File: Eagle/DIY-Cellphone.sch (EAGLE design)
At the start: 66 parts, among them IC1 MEGA1284, J1 ISP, U1 MCP73831, U7 M10_HDWITHOUT_EXCLUSION, X1 BU-SMA-V, X3 CCM03-3002 R102

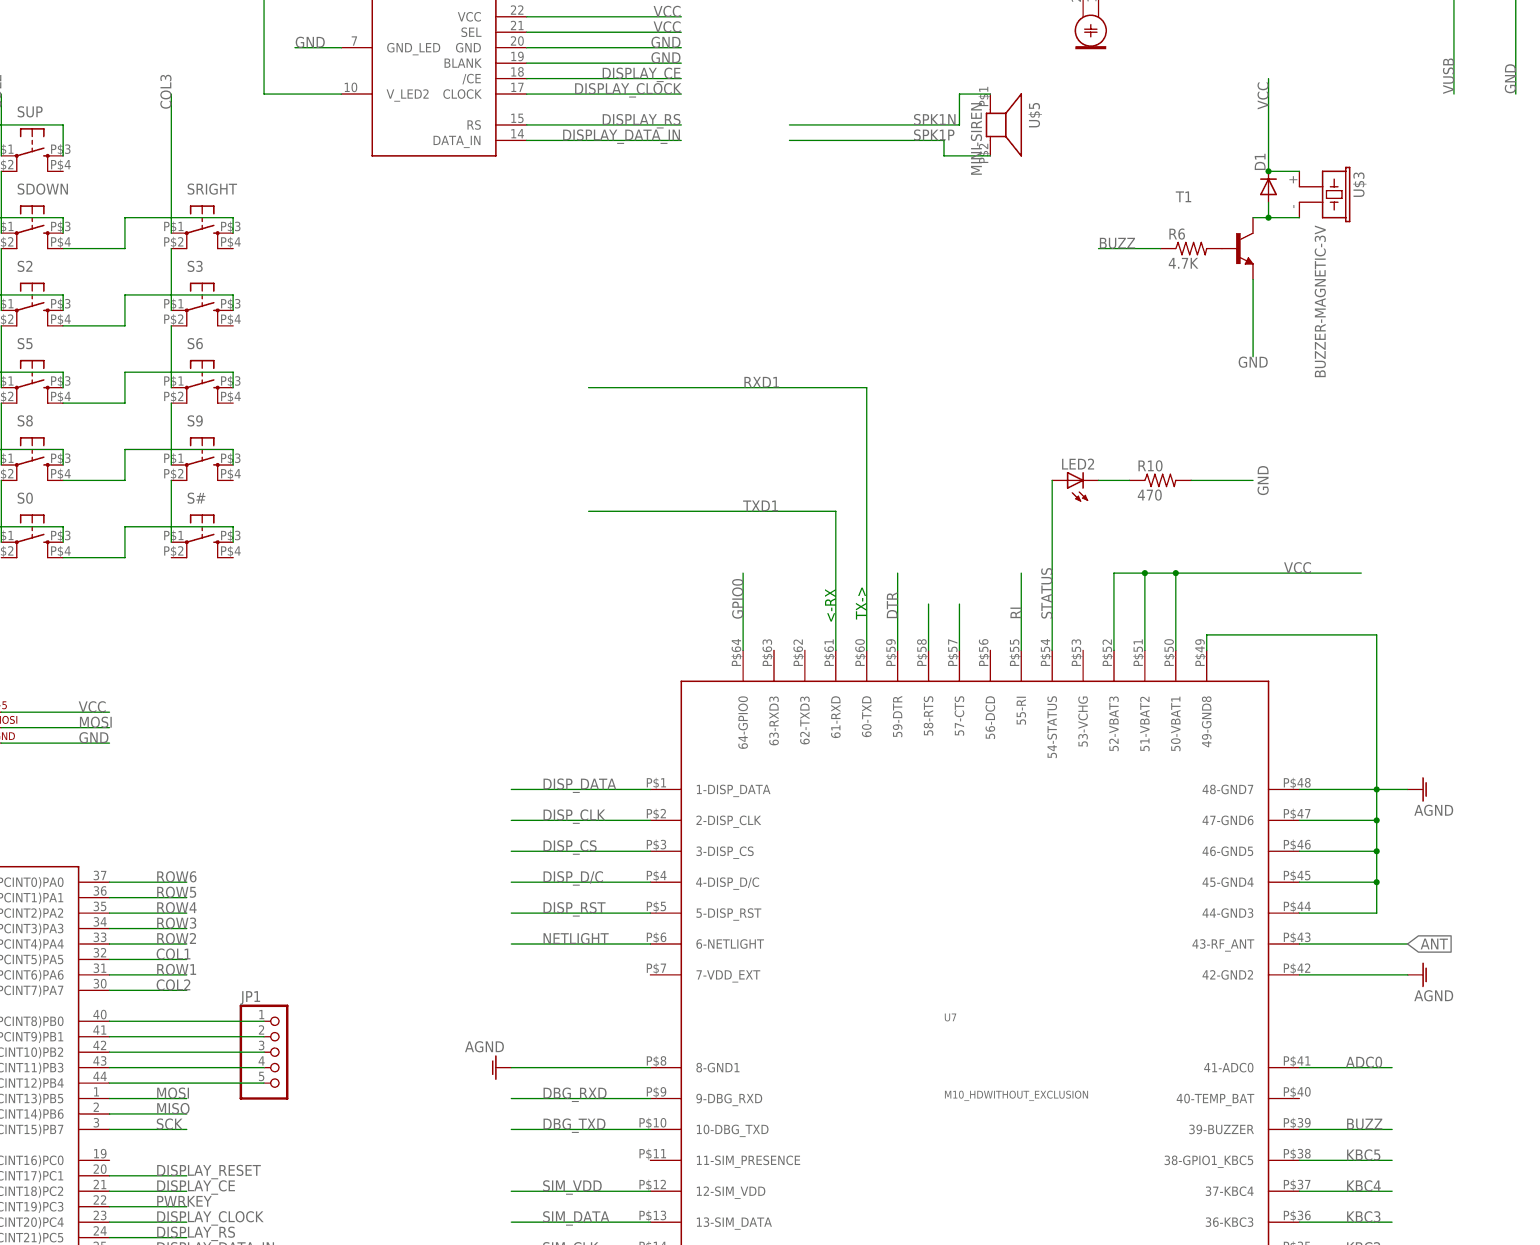
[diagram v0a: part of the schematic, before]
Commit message: Solder jumper to connect buzzer to GSM module or microcontroller (PB4).
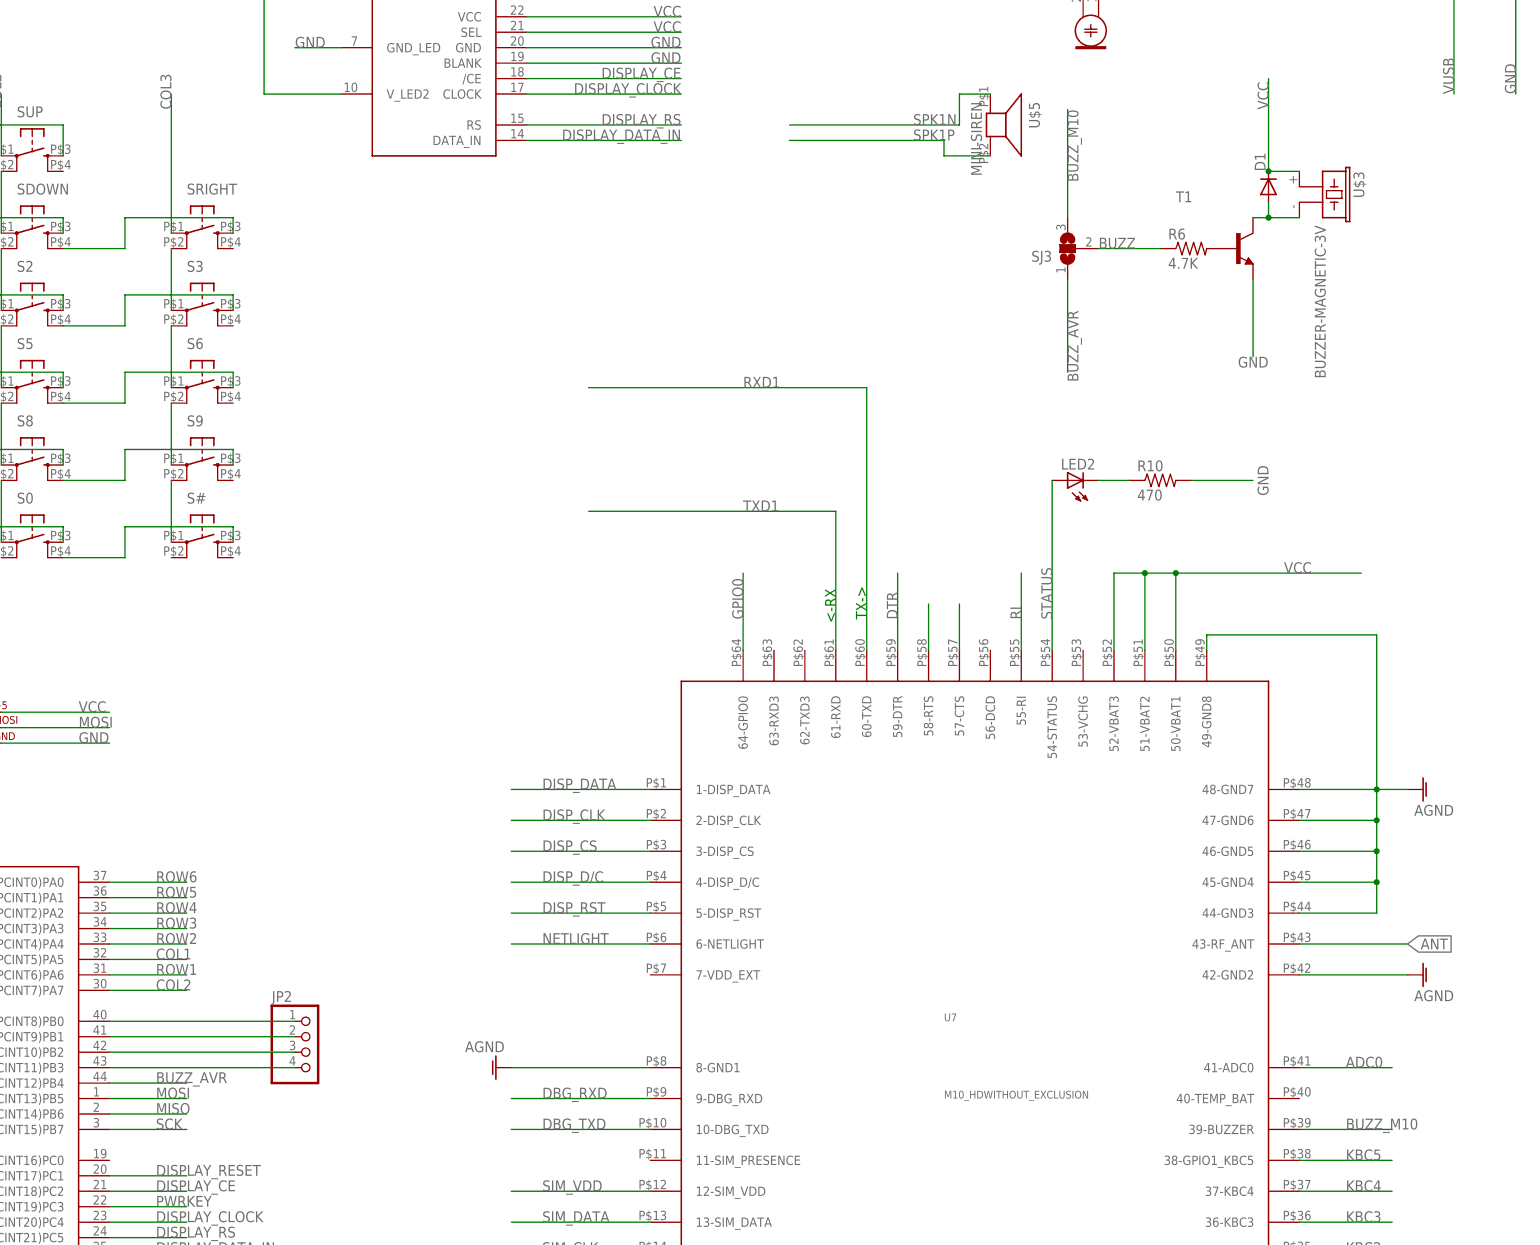
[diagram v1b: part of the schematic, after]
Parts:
- removed JP1: (no value), pinhead:PINHD-1X5
- added JP2: (no value), pinhead:PINHD-1X4
- added SJ3: (no value), jumper:SJ2W
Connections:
- removed net N$42: IC1.(OC0B/!SS!/PCINT12)PB4, JP1.5
- new net BUZZ_AVR: IC1.(OC0B/!SS!/PCINT12)PB4, SJ3.1
- new net BUZZ_M10: SJ3.3, U7.39-BUZZER
- net BUZZ: now also SJ3.2; no longer U7.39-BUZZER
- net N$38: now also JP2.1; no longer JP1.1
- net N$39: now also JP2.2; no longer JP1.2
- net N$40: now also JP2.3; no longer JP1.3
- net N$41: now also JP2.4; no longer JP1.4
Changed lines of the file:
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@@
 <part name="LED2" library="led" deviceset="LED" device="SMT1206"/>
 <part name="R10" library="cellphone-rcl" deviceset="R-US_" device="R1206" value="470"/>
-<part name="JP1" library="pinhead" deviceset="PINHD-1X5" device=""/>
 <part name="U$2" library="cellphone" deviceset="HCMS-[23]97X" device=""/>
+<part name="SJ3" library="jumper" deviceset="SJ2W" device=""/>
+<part name="JP2" library="pinhead" deviceset="PINHD-1X4" device=""/>
 </parts>
 <sheets>
@@
 <instance part="LED2" gate="G$1" x="162.56" y="175.26" rot="R90"/>
 <instance part="R10" gate="G$1" x="177.8" y="175.26"/>
-<instance part="JP1" gate="A" x="33.02" y="81.28"/>
 <instance part="U$2" gate="G$1" x="58.42" y="246.38" rot="R270"/>
+<instance part="SJ3" gate="G$1" x="162.56" y="213.36" rot="R180"/>
+<instance part="JP2" gate="A" x="38.1" y="81.28"/>
 </instances>
 <busses>
@@
 <net name="BUZZ" class="0">
 <segment>
-<wire x1="215.9" y1="68.58" x2="200.66" y2="68.58" width="0.1524" layer="91"/>
-<label x="208.28" y="68.58" size="1.778" layer="95"/>
-<pinref part="U7" gate="G$1" pin="39-BUZZER"/>
-</segment>
-<segment>
 <pinref part="R6" gate="G$1" pin="1"/>
 <wire x1="177.8" y1="213.36" x2="167.64" y2="213.36" width="0.1524" layer="91"/>
 <label x="167.64" y="213.36" size="1.778" layer="95"/>
+<pinref part="SJ3" gate="G$1" pin="2"/>
 </segment>
 </net>
@@
 <segment>
 <pinref part="IC1" gate="G$1" pin="(XCK0/T0/PCINT8)PB0"/>
-<pinref part="JP1" gate="A" pin="1"/>
-<wire x1="30.48" y1="86.36" x2="5.08" y2="86.36" width="0.1524" layer="91"/>
+<pinref part="JP2" gate="A" pin="1"/>
+<wire x1="35.56" y1="86.36" x2="5.08" y2="86.36" width="0.1524" layer="91"/>
 </segment>
 </net>
@@
 <segment>
 <pinref part="IC1" gate="G$1" pin="(CLKO/T1/PCINT9)PB1"/>
-<pinref part="JP1" gate="A" pin="2"/>
-<wire x1="30.48" y1="83.82" x2="5.08" y2="83.82" width="0.1524" layer="91"/>
+<pinref part="JP2" gate="A" pin="2"/>
+<wire x1="35.56" y1="83.82" x2="5.08" y2="83.82" width="0.1524" layer="91"/>
 </segment>
 </net>
@@
 <segment>
 <pinref part="IC1" gate="G$1" pin="(INT2/AIN0/PCINT10)PB2"/>
-<pinref part="JP1" gate="A" pin="3"/>
-<wire x1="30.48" y1="81.28" x2="5.08" y2="81.28" width="0.1524" layer="91"/>
+<pinref part="JP2" gate="A" pin="3"/>
+<wire x1="35.56" y1="81.28" x2="5.08" y2="81.28" width="0.1524" layer="91"/>
 </segment>
 </net>
@@
 <segment>
 <pinref part="IC1" gate="G$1" pin="(OC0A/AIN1/PCINT11)PB3"/>
-<pinref part="JP1" gate="A" pin="4"/>
-<wire x1="30.48" y1="78.74" x2="5.08" y2="78.74" width="0.1524" layer="91"/>
-</segment>
-</net>
-<net name="N$42" class="0">
+<pinref part="JP2" gate="A" pin="4"/>
+<wire x1="35.56" y1="78.74" x2="5.08" y2="78.74" width="0.1524" layer="91"/>
+</segment>
+</net>
+<net name="BUZZ_AVR" class="0">
 <segment>
 <pinref part="IC1" gate="G$1" pin="(OC0B/!SS!/PCINT12)PB4"/>
-<pinref part="JP1" gate="A" pin="5"/>
-<wire x1="30.48" y1="76.2" x2="5.08" y2="76.2" width="0.1524" layer="91"/>
+<wire x1="17.78" y1="76.2" x2="5.08" y2="76.2" width="0.1524" layer="91"/>
+<label x="12.7" y="76.2" size="1.778" layer="95"/>
+</segment>
+<segment>
+<pinref part="SJ3" gate="G$1" pin="1"/>
+<wire x1="162.56" y1="208.28" x2="162.56" y2="193.04" width="0.1524" layer="91"/>
+<label x="162.56" y="203.2" size="1.778" layer="95" rot="R270"/>
 </segment>
 </net>
@@
 </segment>
 </net>
+<net name="BUZZ_M10" class="0">
+<segment>
+<pinref part="SJ3" gate="G$1" pin="3"/>
+<wire x1="162.56" y1="218.44" x2="162.56" y2="236.22" width="0.1524" layer="91"/>
+<label x="162.56" y="236.22" size="1.778" layer="95" rot="R270"/>
+</segment>
+<segment>
+<wire x1="215.9" y1="68.58" x2="200.66" y2="68.58" width="0.1524" layer="91"/>
+<label x="208.28" y="68.58" size="1.778" layer="95"/>
+<pinref part="U7" gate="G$1" pin="39-BUZZER"/>
+</segment>
+</net>
